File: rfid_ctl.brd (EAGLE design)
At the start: 42.5 x 52.2 mm, 39 parts, among them Q1 FDS5680, Q2 FDS5680, SW2 L202011MS02Q, U1 MC34063SMD, X2 1503_02

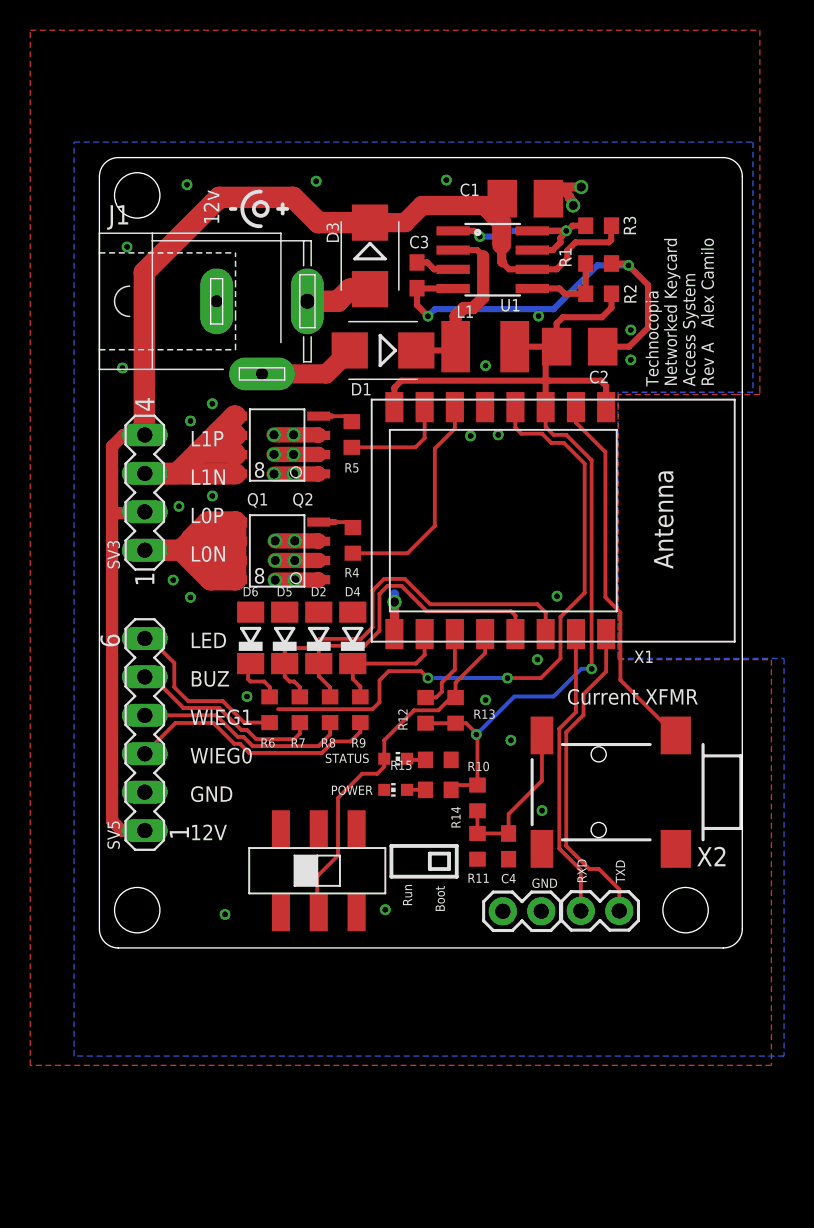
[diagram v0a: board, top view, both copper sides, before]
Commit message: GPIO pulled low and HP jack swapped with something sourcable
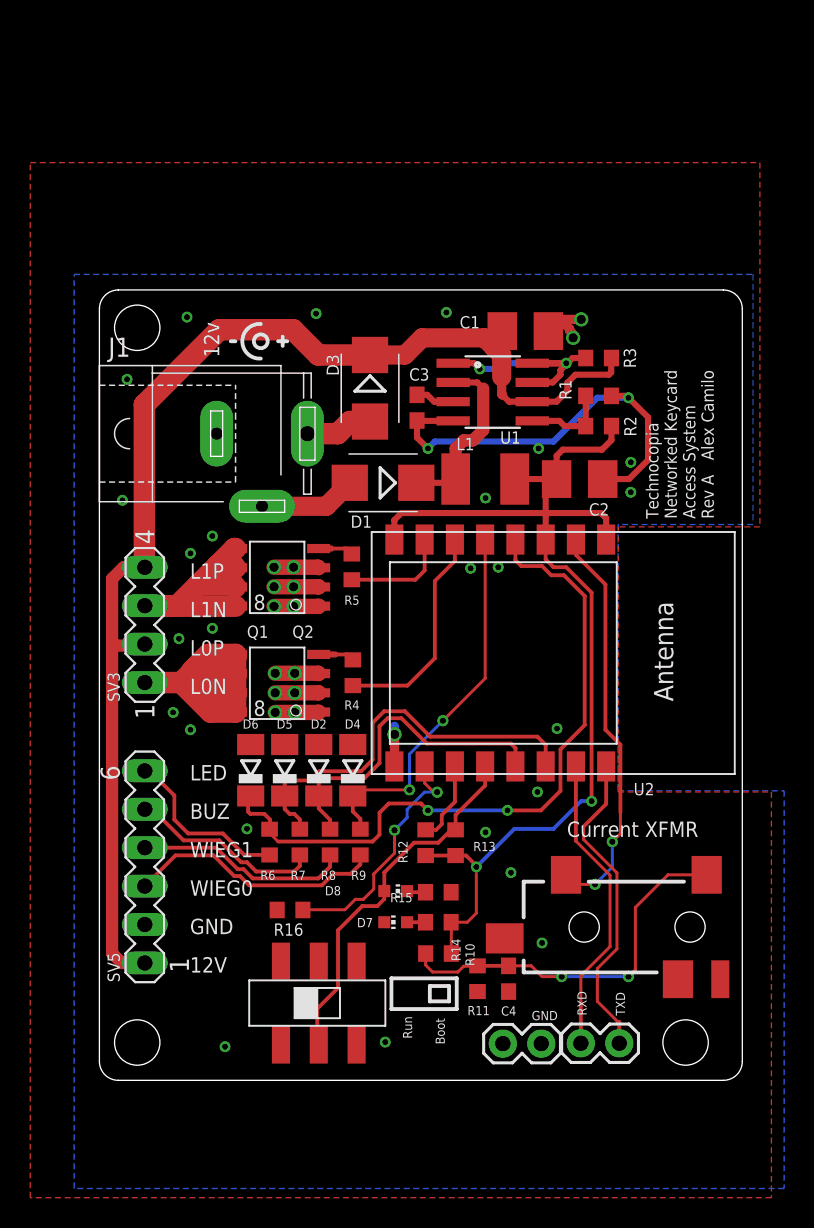
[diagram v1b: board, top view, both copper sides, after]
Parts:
- removed JP2: M02PTH, SparkFun-Connectors:1X02
- removed POWER, STATUS: (no value), adafruit:CHIP-LED0603
- removed X1: (no value), adafruit:ESP-12
- removed X2: 1503_02, con-lumberg:1503_02
- added D7, D8: (no value), adafruit:CHIP-LED0603
- added J2, J3: M02PTH, SparkFun-Connectors:1X02
- added R16: 10k, rcl:R0603
- added U2: (no value), adafruit:ESP-12
- C2: value (none) -> 22uF
- C3: value (none) -> 130pf
- C4: value (none) -> 0.1uF
- D1, D2, D3, D4, D5, D6: value 1N5859 -> (none)
- JP1: value M02PTH -> (none); device SparkFun-Connectors:1X02 -> SparkFun-Connectors:AUDIO-JACK-3.5MM-SMD
- R10, R11, R12, R13: value 0R33 -> 10k
- R14, R15: value 0R33 -> 330
- R3: value 0R33 -> 0.5
- R4, R5, R6, R7, R8, R9: value 0R33 -> 33
- moved R10 10.6 mm to (22.4, 8.38), turned to 0 degrees
- moved C1 8.75 mm to (28.2, 49.5)
- moved C2 8.75 mm to (31.8, 39.8)
- moved C3 8.75 mm to (21.0, 44.5)
- moved C4 8.75 mm to (27.1, 6.72)
- moved D1 8.75 mm to (18.8, 39.5)
- moved D2 8.75 mm to (14.5, 20.5)
- moved D3 8.75 mm to (17.9, 45.8)
- moved D4 8.75 mm to (16.8, 20.5)
- moved D5 8.75 mm to (12.2, 20.5)
- moved D6 8.75 mm to (10.0, 20.5)
- moved J1 8.75 mm to (10.8, 42.8)
- moved L1 8.75 mm to (25.5, 39.8)
- moved Q1 8.75 mm to (11.8, 26.2)
- moved Q2 8.75 mm to (11.8, 33.2)
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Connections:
- new net GP15: R16.1, U2.10
- net +3V3: now also U2.1, U2.3, U2.8; no longer X1.1, X1.3, X1.8
- net BUZZ: now also U2.14; no longer X1.14
- net CURR: now also JP1.TIP, U2.2; no longer X1.2, X2.2
- net ESP_RXD: now also J2.2, U2.15; no longer JP1.2, X1.15
- net ESP_TXD: now also J2.1, U2.16; no longer JP1.1, X1.16
- net GND: now also D7.C, J3.1, J3.2, R16.2, U2.9; no longer JP2.1, JP2.2, POWER.C, X1.9
- net GP0: now also D8.A, U2.12; no longer STATUS.A, X1.12
- net GP2: now also U2.11; no longer X1.11
- net L0NS: now also U2.6; no longer X1.6
- net L1NS: now also U2.7; no longer X1.7
- net LED: now also U2.4; no longer X1.4
- net N$12: now also JP1.SLEEVE; no longer X2.1
- net N$13: now also D7.A; no longer POWER.A
- net N$14: now also D8.C; no longer STATUS.C
- net WIEG0: now also U2.5; no longer X1.10
- net WIEG1: now also U2.13; no longer X1.13
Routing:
- net WIEG0: track 8.77 -> 24.9 mm, vias 0 -> 2
- net GP15: track 0.00 -> 16.1 mm, vias 0 -> 2
- net N$12: track 11.0 -> 25.4 mm, vias 0 -> 2
- net CURR: track 24.4 -> 26.9 mm, vias 0 -> 2
- net +3V3: track 67.9 -> 70.1 mm
- net LED: track 45.3 -> 46.3 mm
- net ESP_RXD: track 19.3 -> 20.0 mm

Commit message: more cleanup
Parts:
- moved C4 0.92 mm to (27.0, 5.80)
- moved R11 0.92 mm to (24.9, 5.80)
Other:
- board text added: "Technocopia Networked Keycard Access System Rev B Alex Camilo"
- board text removed: "Technocopia Networked Keycard Access System Rev A Alex Camilo"
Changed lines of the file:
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@@
 Networked Keycard
 Access System
-Rev A   Alex Camilo</text>
+Rev B   Alex Camilo</text>
 <text x="7.9248" y="47.7904" size="1.016" layer="21" font="vector" rot="R90">12v</text>
 <wire x1="10.668" y1="47.7142" x2="10.668" y2="50.0002" width="0.254" layer="21" curve="-187.62815"/>
@@
 <attribute name="NAME" x="24.8034" y="7.5692" size="0.6096" layer="25" font="vector" rot="R90"/>
 </element>
-<element name="R11" library="rcl" package="R0603" value="10k" x="24.9936" y="6.7186" smashed="yes" rot="R90">
-<attribute name="NAME" x="25.8064" y="4.9152" size="0.6096" layer="25" font="vector" rot="R180"/>
-</element>
-<element name="C4" library="rcl" package="C0603" value="0.1uF" x="27.051" y="6.7186" smashed="yes" rot="R90">
-<attribute name="NAME" x="27.559" y="4.8898" size="0.6096" layer="25" font="vector" rot="R180"/>
-<attribute name="VALUE" x="29.083" y="5.8296" size="1.27" layer="27" rot="R90"/>
+<element name="R11" library="rcl" package="R0603" value="10k" x="24.9174" y="5.8042" smashed="yes" rot="R90">
+<attribute name="NAME" x="25.7302" y="4.0008" size="0.6096" layer="25" font="vector" rot="R180"/>
+</element>
+<element name="C4" library="rcl" package="C0603" value="0.1uF" x="26.9748" y="5.8042" smashed="yes" rot="R90">
+<attribute name="NAME" x="27.4828" y="3.9754" size="0.6096" layer="25" font="vector" rot="R180"/>
+<attribute name="VALUE" x="29.0068" y="4.9152" size="1.27" layer="27" rot="R90"/>
 </element>
 <element name="J2" library="SparkFun-Connectors" package="1X02" value="M02PTH" x="34.3662" y="2.4514" smashed="yes" rot="R180"/>
@@
 <contactref element="R10" pad="1"/>
 <contactref element="R11" pad="2"/>
-<wire x1="24.9936" y1="7.7092" x2="24.9936" y2="7.5686" width="0.254" layer="1"/>
-<wire x1="24.9936" y1="7.7092" x2="25.1342" y2="7.5686" width="0.254" layer="1"/>
-<wire x1="25.1342" y1="7.5686" x2="27.051" y2="7.5686" width="0.254" layer="1"/>
 <contactref element="JP1" pad="SLEEVE"/>
 <wire x1="21.5658" y1="8.382" x2="21.5658" y2="7.6188" width="0.2" layer="1"/>
 <wire x1="21.5658" y1="7.6188" x2="22.0218" y2="7.1628" width="0.2" layer="1"/>
 <wire x1="22.0218" y1="7.1628" x2="23.6982" y2="7.1628" width="0.2" layer="1"/>
-<wire x1="23.6982" y1="7.1628" x2="24.0792" y2="7.5438" width="0.2" layer="1"/>
-<wire x1="24.0792" y1="7.5438" x2="24.9688" y2="7.5438" width="0.2" layer="1"/>
-<wire x1="24.9688" y1="7.5438" x2="24.9936" y2="7.5686" width="0.2" layer="1"/>
 <wire x1="40.145" y1="13.5846" x2="37.5876" y2="13.5846" width="0.2" layer="1"/>
 <wire x1="37.5876" y1="13.5846" x2="35.433" y2="11.43" width="0.2" layer="1"/>
@@
 <wire x1="34.9758" y1="6.858" x2="30.5562" y2="6.858" width="0.2" layer="16"/>
 <via x="30.5562" y="6.858" extent="1-16" drill="0.4"/>
-<wire x1="30.5562" y1="6.858" x2="29.2608" y2="6.858" width="0.2" layer="1"/>
-<wire x1="29.2608" y1="6.858" x2="28.5502" y2="7.5686" width="0.2" layer="1"/>
-<wire x1="28.5502" y1="7.5686" x2="27.051" y2="7.5686" width="0.2" layer="1"/>
+<wire x1="30.5562" y1="6.858" x2="29.9466" y2="6.858" width="0.2" layer="1"/>
+<wire x1="29.9466" y1="6.858" x2="29.2608" y2="6.858" width="0.2" layer="1"/>
+<wire x1="24.9174" y1="6.6542" x2="26.9748" y2="6.6542" width="0.2032" layer="1"/>
+<wire x1="23.6982" y1="7.1628" x2="24.2068" y2="6.6542" width="0.2032" layer="1"/>
+<wire x1="24.2068" y1="6.6542" x2="24.9174" y2="6.6542" width="0.2032" layer="1"/>
+<wire x1="26.9748" y1="6.6542" x2="27.1786" y2="6.858" width="0.2032" layer="1"/>
+<wire x1="27.1786" y1="6.858" x2="29.9466" y2="6.858" width="0.2032" layer="1"/>
 </signal>
 <signal name="CURR">
